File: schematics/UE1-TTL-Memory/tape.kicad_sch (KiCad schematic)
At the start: 10 parts, among them SW2 Select Program, U7 74LS393, U8 74LS393, U9 28C256

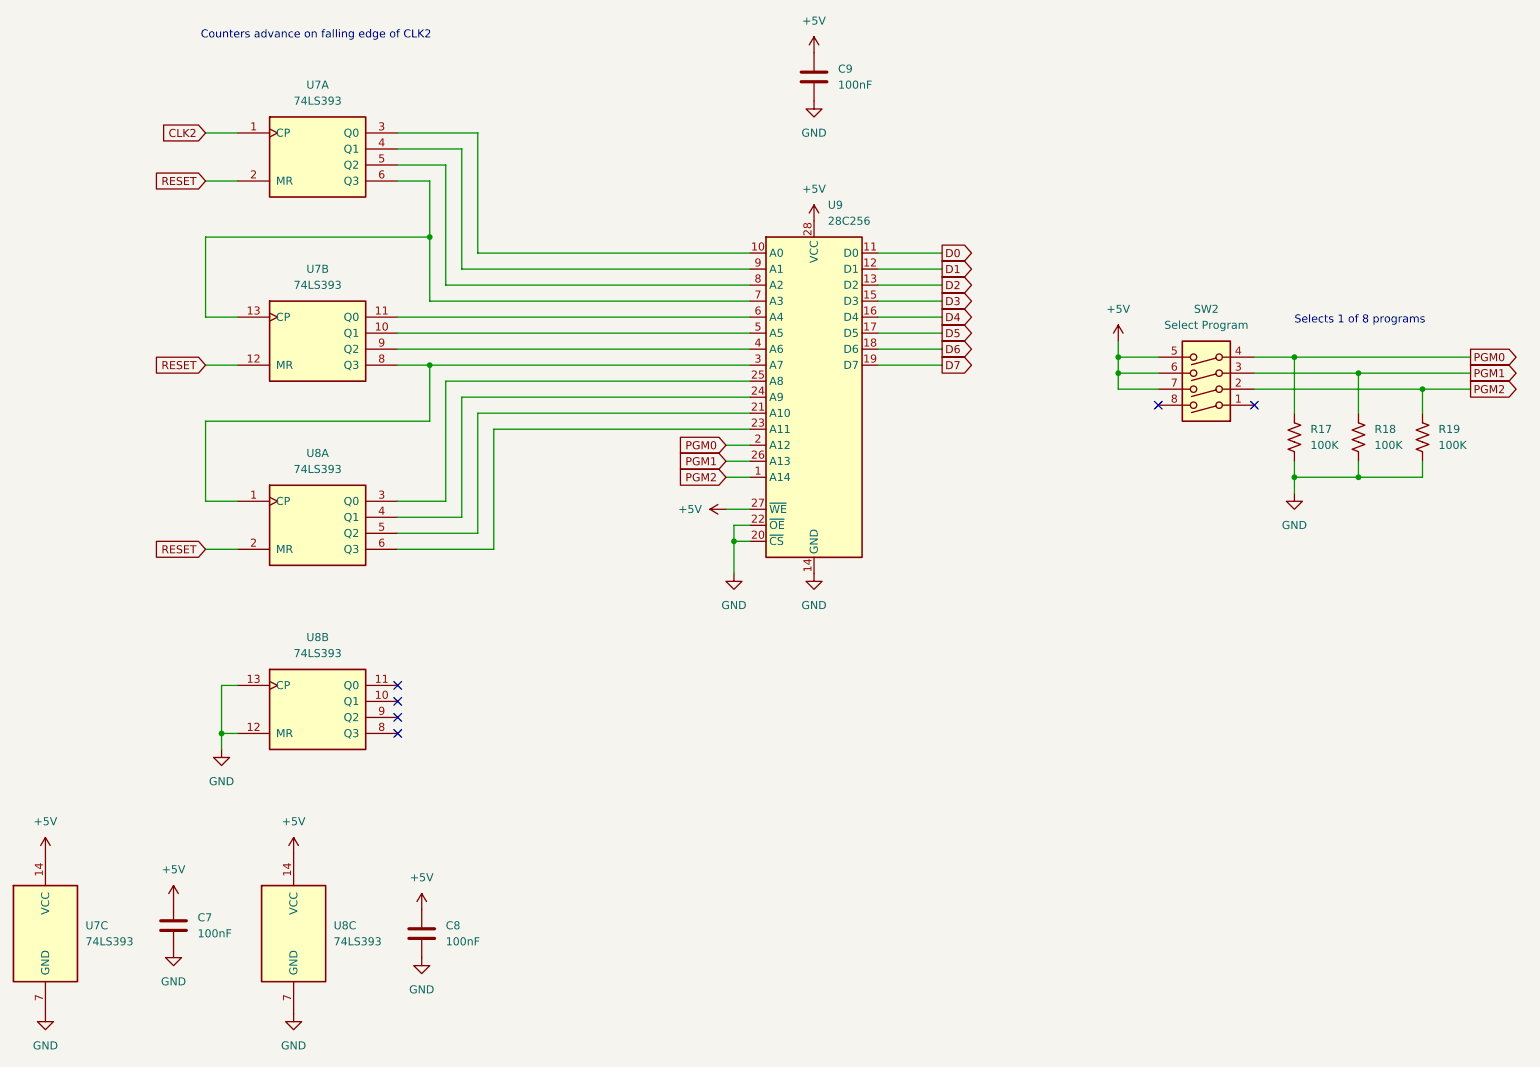
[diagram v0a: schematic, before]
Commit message: Add a tape "REWIND" opcode to reset the PC early
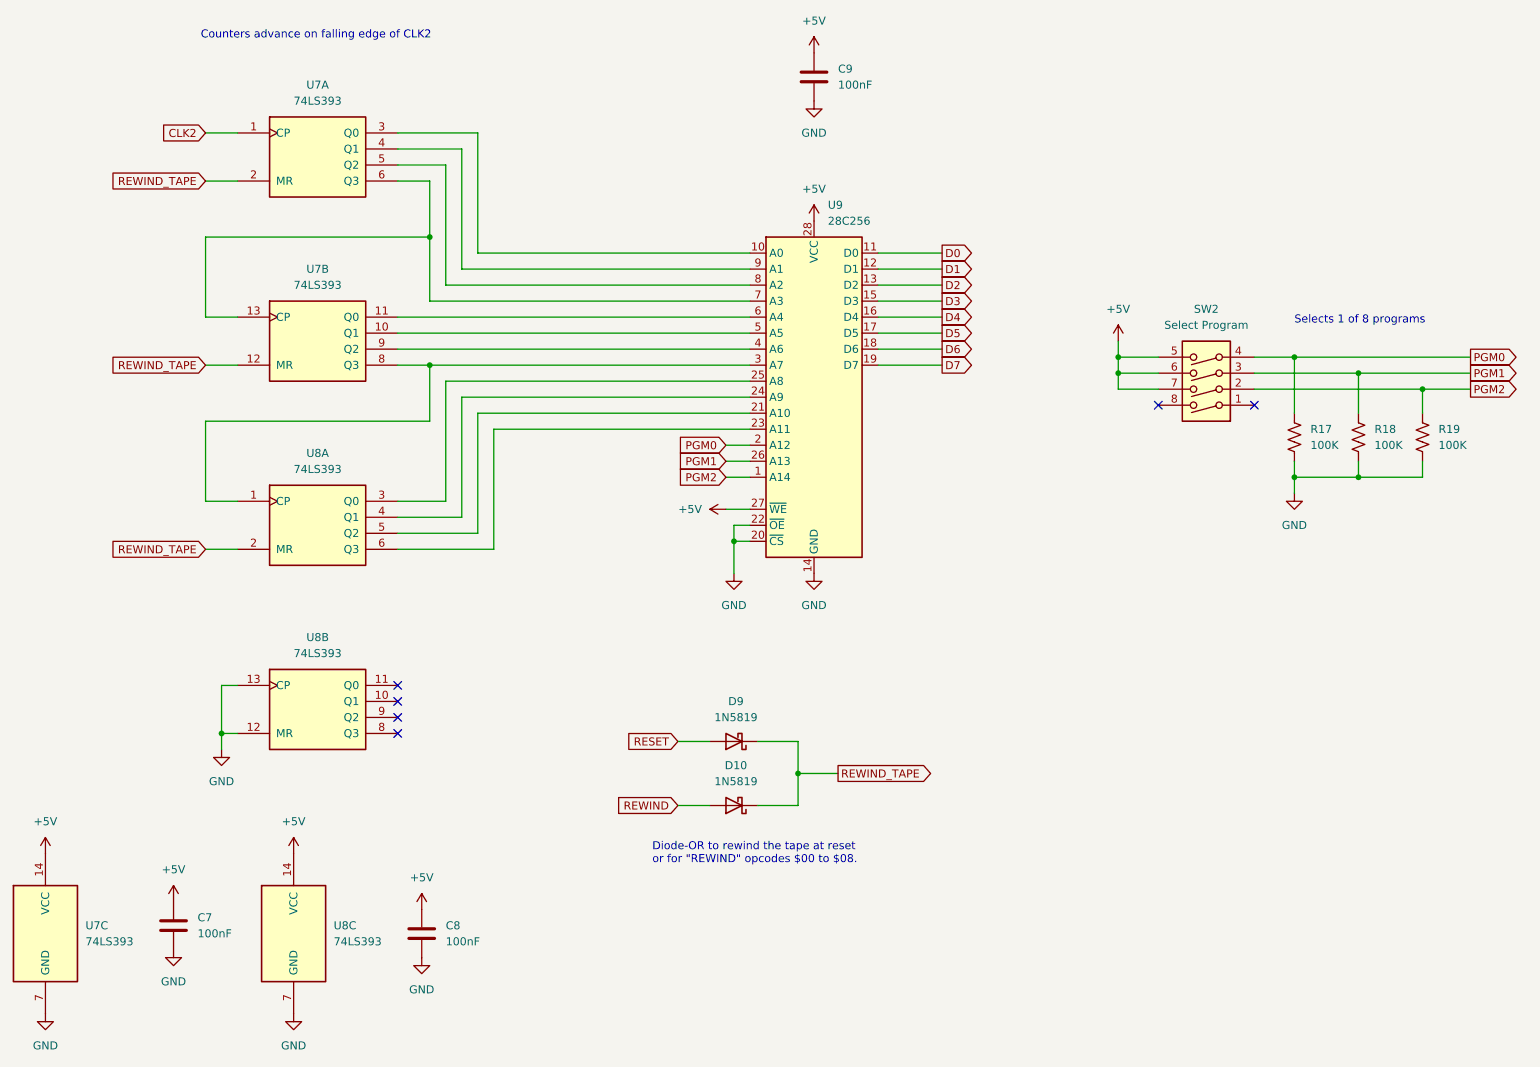
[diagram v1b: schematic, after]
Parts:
- added D10, D9: 1N5819, Diode_THT:D_DO-41_SOD81_P10.16mm_Horizontal, symbol Diode:1N5819
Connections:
- net RESET: now also D9.2 (A); no longer U7.12 (MR), U7.2 (MR), U8.2 (MR)
- new net REWIND: D10.2 (A)
- new net REWIND_TAPE: D10.1 (K), D9.1 (K), U7.12 (MR), U7.2 (MR), U8.2 (MR)
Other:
- note added: "Diode-OR to rewind the tape at reset or for "REWIND" opcodes $00 to $08."

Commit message: Lay out memory board
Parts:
- removed D10, D9: 1N5819, Diode_THT:D_DO-41_SOD81_P10.16mm_Horizontal, symbol Diode:1N5819
- removed SW2: Select Program, Button_Switch_THT:SW_DIP_SPSTx04_Slide_9.78x12.34mm_W7.62mm_P2.54mm, symbol Switch:SW_DIP_x04
- added C8: 100nF, Capacitor_THT:C_Disc_D5.0mm_W2.5mm_P5.00mm, symbol Device:C
- added SW2: Select Program, Button_Switch_THT:SW_DIP_SPSTx03_Slide_6.7x9.18mm_W7.62mm_P2.54mm_LowProfile, symbol Switch:SW_DIP_x03
- added U8: 74LS32, Package_DIP:DIP-14_W7.62mm, symbol 74xx:74LS32
- renumbered C7 to C6, C8 to C7, U7 to U6, U8 to U7
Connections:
- net +5V: now also C8.1, SW2.4, SW2.5, SW2.6, U8.14 (VCC)
- net GND: now also C8.2, U8.1, U8.12, U8.13, U8.2, U8.4, U8.5, U8.7 (GND)
- net PGM0: now also SW2.3
- net PGM1: now also SW2.2
- net PGM2: now also SW2.1
- net RESET: now also U8.9
- net REWIND: now also U8.10
- net REWIND_TAPE: now also U8.8
- no-connect marks 6 -> 7
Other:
- note removed: "Diode-OR to rewind the tape at reset or for "REWIND" opcodes $00 to $08."
